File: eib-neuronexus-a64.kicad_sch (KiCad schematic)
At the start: 4 parts, among them J1 xOLC-110-01-S-Q_1, J2 xOLC-110-01-S-Q_1, J3 Conn_02x35_Odd_Even, J4 Conn_01x02_Male

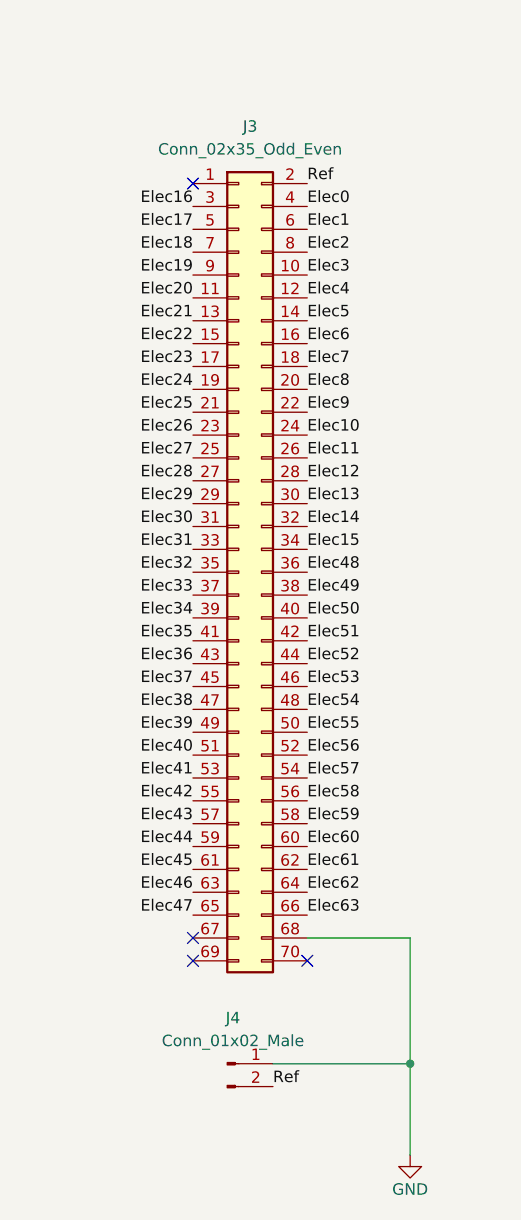
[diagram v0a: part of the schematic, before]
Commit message: Revision B
- Fixed pinout to match 1.3B headstage-64
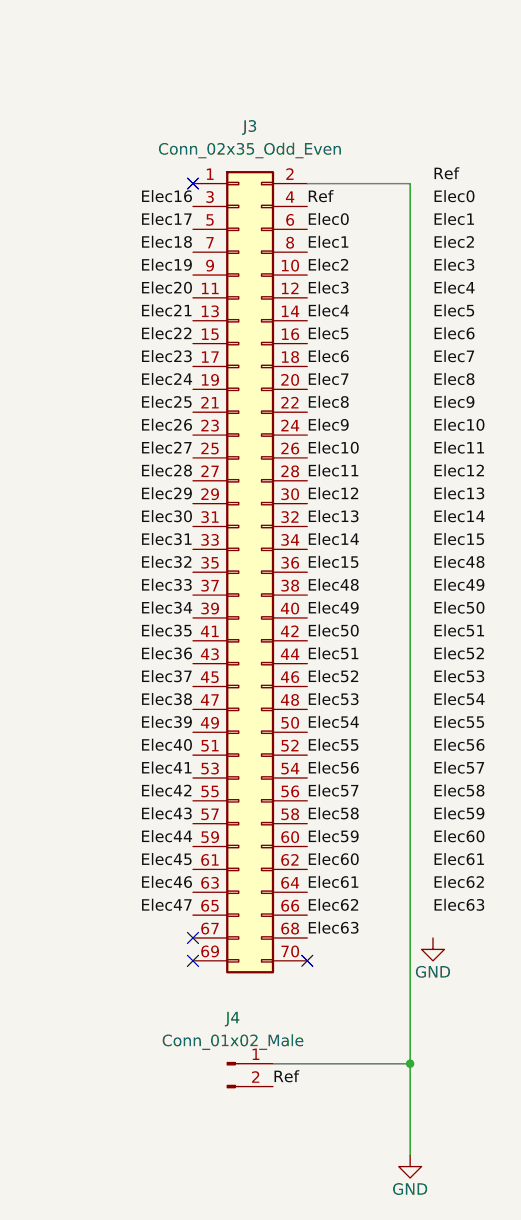
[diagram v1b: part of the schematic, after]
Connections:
- net Elec0: now also J3.6 (Pin_6); no longer J3.4 (Pin_4)
- net Elec1: now also J3.8 (Pin_8); no longer J3.6 (Pin_6)
- net Elec10: now also J3.26 (Pin_26); no longer J3.24 (Pin_24)
- net Elec11: now also J3.28 (Pin_28); no longer J3.26 (Pin_26)
- net Elec12: now also J3.30 (Pin_30); no longer J3.28 (Pin_28)
- net Elec13: now also J3.32 (Pin_32); no longer J3.30 (Pin_30)
- net Elec14: now also J3.34 (Pin_34); no longer J3.32 (Pin_32)
- net Elec15: now also J3.36 (Pin_36); no longer J3.34 (Pin_34)
- net Elec2: now also J3.10 (Pin_10); no longer J3.8 (Pin_8)
- net Elec3: now also J3.12 (Pin_12); no longer J3.10 (Pin_10)
- net Elec4: now also J3.14 (Pin_14); no longer J3.12 (Pin_12)
- net Elec48: now also J3.38 (Pin_38); no longer J3.36 (Pin_36)
- net Elec49: now also J3.40 (Pin_40); no longer J3.38 (Pin_38)
- net Elec5: now also J3.16 (Pin_16); no longer J3.14 (Pin_14)
- net Elec50: now also J3.42 (Pin_42); no longer J3.40 (Pin_40)
- net Elec51: now also J3.44 (Pin_44); no longer J3.42 (Pin_42)
- net Elec52: now also J3.46 (Pin_46); no longer J3.44 (Pin_44)
- net Elec53: now also J3.48 (Pin_48); no longer J3.46 (Pin_46)
- net Elec54: now also J3.50 (Pin_50); no longer J3.48 (Pin_48)
- net Elec55: now also J3.52 (Pin_52); no longer J3.50 (Pin_50)
- net Elec56: now also J3.54 (Pin_54); no longer J3.52 (Pin_52)
- net Elec57: now also J3.56 (Pin_56); no longer J3.54 (Pin_54)
- net Elec58: now also J3.58 (Pin_58); no longer J3.56 (Pin_56)
- net Elec59: now also J3.60 (Pin_60); no longer J3.58 (Pin_58)
- net Elec6: now also J3.18 (Pin_18); no longer J3.16 (Pin_16)
- net Elec60: now also J3.62 (Pin_62); no longer J3.60 (Pin_60)
- net Elec61: now also J3.64 (Pin_64); no longer J3.62 (Pin_62)
- net Elec62: now also J3.66 (Pin_66); no longer J3.64 (Pin_64)
- net Elec63: now also J3.68 (Pin_68); no longer J3.66 (Pin_66)
- net Elec7: now also J3.20 (Pin_20); no longer J3.18 (Pin_18)
- net Elec8: now also J3.22 (Pin_22); no longer J3.20 (Pin_20)
- net Elec9: now also J3.24 (Pin_24); no longer J3.22 (Pin_22)
- net GND: now also J3.2 (Pin_2); no longer J3.68 (Pin_68)
- net Ref: now also J3.4 (Pin_4); no longer J3.2 (Pin_2)
